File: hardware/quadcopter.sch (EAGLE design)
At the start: 92 parts, among them J1 HEADER-4POS-0.1IN-FEMALE-SMD-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, J2 HEADER-10POSTH-254X10, J3 HEADER-4POS-0.1IN-FEMALE, J4 AVR_SPI_PRG_6-SMD, M1 MOTOR_PADS_GND-MOLEX-SMD, M2 MOTOR_PADS_GND-MOLEX-SMD, M3 MOTOR_PADS_GND-MOLEX-SMD, M4 MOTOR_PADS_GND-MOLEX-SMD, Q1 N-MOSFET-SI2302DS, Q10 N-MOSFET-SI2302DS, Q11 N-MOSFET-SI2302DS, Q12 N-MOSFET-SI2302DS, Q2 N-MOSFET-SI2302DS, Q3 N-MOSFET-SI2302DS, Q4 N-MOSFET-SI2302DS, Q5 N-MOSFET-SI2302DS, Q6 N-MOSFET-SI2302DS, Q7 N-MOSFET-SI2302DS, Q8 N-MOSFET-SI2302DS, Q9 N-MOSFET-SI2302DS, SW1 PUSHBUTTON_-4.5X4.5, U1 ATMEGA128RFA1, U2 IMU_LSM9DS1-LSM9DS1, Y1 CRYSTAL5X3

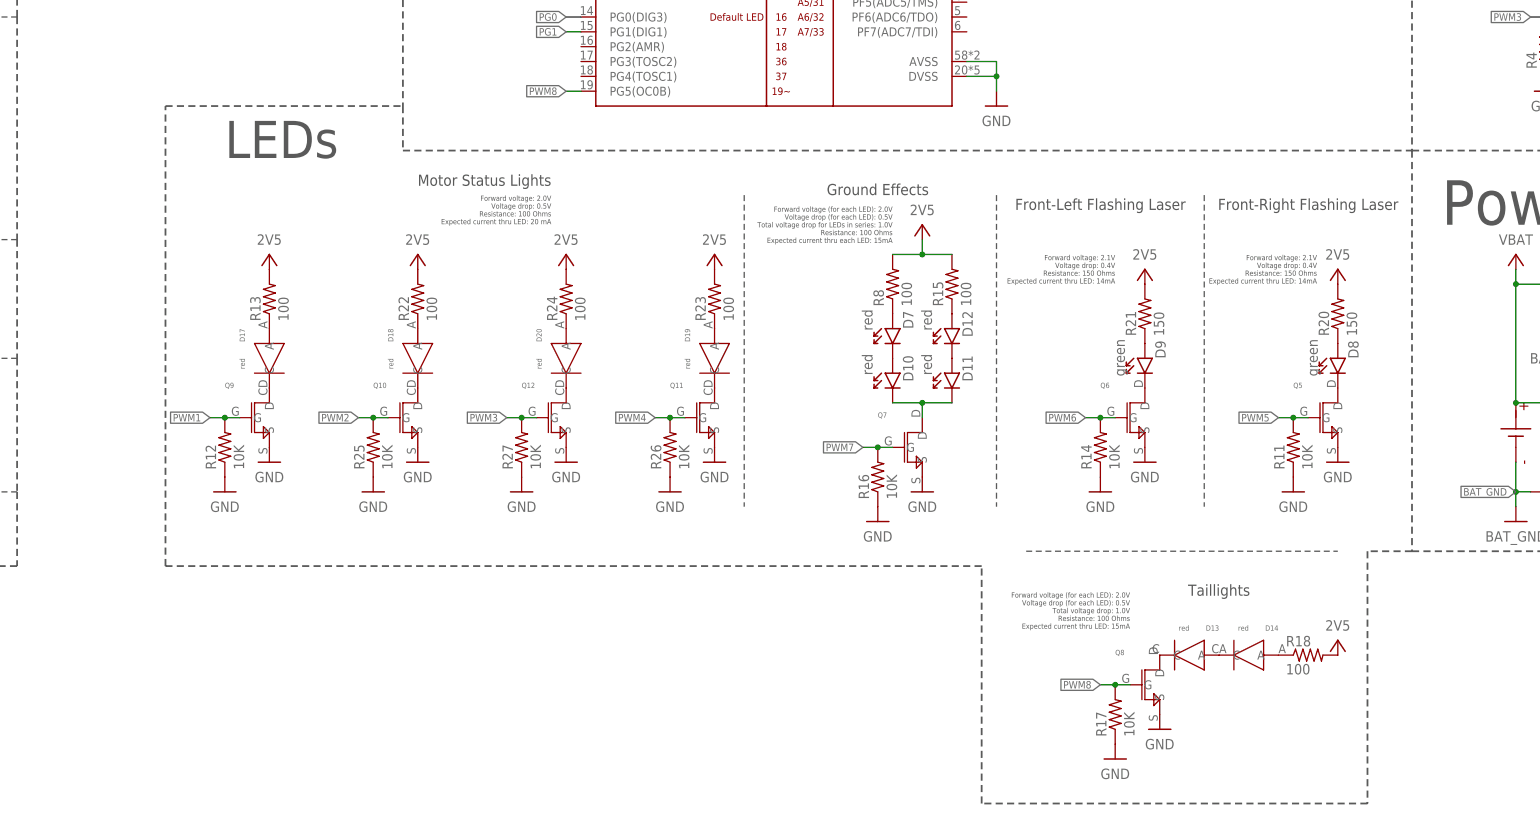
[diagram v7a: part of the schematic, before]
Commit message: Modify LED schematic to meet lab specs
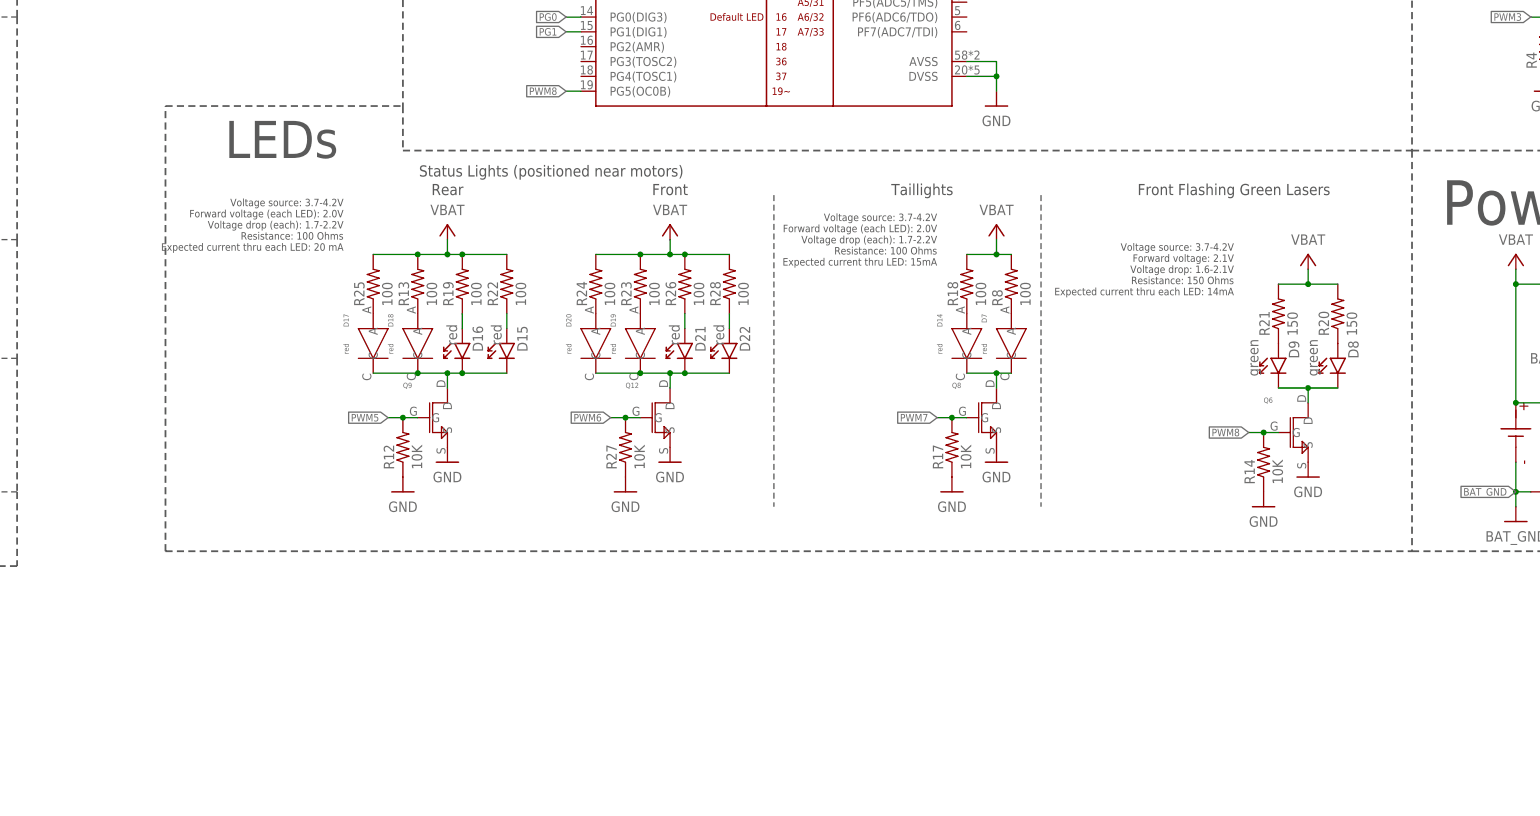
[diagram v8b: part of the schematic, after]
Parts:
- removed D10, D11, D12: red, LED:LED-350-2312-1-ND-REVERSE
- removed D13: red, custom_michael_shao:LED_RED-LTST-C170EKT
- removed Q10, Q11, Q5, Q7: N-MOSFET-SI2302DS, custom_michael_shao:N-MOSFET-SI2302DS
- removed R11, R16: 10K, quadparts_prebuilt_2022:RESISTOR_SMD-2012-0805-10K
- removed R15: 100, quadparts_prebuilt_2022:RESISTOR_SMD-2012-0805-100
- added D15, D16, D21, D22: red, LED:LED-350-2312-1-ND-REVERSE
- added R19, R28: 100, quadparts_prebuilt_2022:RESISTOR_SMD-2012-0805-100
- D7: device LED:LED-350-2312-1-ND-REVERSE -> custom_michael_shao:LED_RED-LTST-C170EKT
- R25, R26: value 10K -> 100; device quadparts_prebuilt_2022:RESISTOR_SMD-2012-0805-10K -> quadparts_prebuilt_2022:RESISTOR_SMD-2012-0805-100
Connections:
- removed net N$18 (its old number): D8.C, Q5.D
- removed net N$21 (its old number): D9.C, Q6.D
- removed net N$28: D11.A, D12.C
- removed net N$29: D13.A, D14.C
- removed net N$30: D10.C, D11.C, Q7.D
- removed net N$32: D13.C, Q8.D
- removed net N$33: D12.A, R15.1
- removed net N$36: D17.A, R13.1
- removed net N$37: D18.A, R22.1
- removed net N$41: D19.C, Q11.D
- new net N$17: D8.C, D9.C, Q6.D
- new net N$24: D17.A, R25.1
- new net N$25: D18.A, R13.1
- new net N$26: D16.A, R19.1
- new net N$34: D15.A, R22.1
- new net N$43: D22.A, R28.1
- net 2V5: no longer R13.2, R15.2, R18.2, R20.2, R21.2, R22.2, R23.2, R24.2, R8.2
- net GND: no longer Q10.S, Q11.S, Q5.S, Q7.S, R11.1, R16.1, R25.1, R26.1
- net N$27: now also D14.C, Q8.D; no longer D10.A
- net N$35: now also D15.C, D16.C, D18.C
- net N$40: now also D19.C, D20.C, D21.C, D22.C, Q12.D; no longer D18.C, Q10.D
- net N$42: now also D21.A, R26.1; no longer D20.C, Q12.D
- net PWM1: no longer Q9.G, R12.2
- net PWM2: no longer Q10.G, R25.2
- net PWM3: no longer Q12.G, R27.2
- net PWM4: no longer Q11.G, R26.2
- net PWM5: now also Q9.G, R12.2; no longer Q5.G, R11.2
- net PWM6: now also Q12.G, R27.2; no longer Q6.G, R14.2
- net PWM7: now also Q8.G, R17.2; no longer Q7.G, R16.2
- net PWM8: now also Q6.G, R14.2; no longer Q8.G, R17.2
- net VBAT: now also R13.2, R18.2, R19.2, R20.2, R21.2, R22.2, R23.2, R24.2, R25.2, R26.2, R28.2, R8.2
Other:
- note added: "Front"
- note added: "Front Flashing Green Lasers"
- note added: "Rear"
- note added: "Status Lights (positioned near motors)"
- note added: "Voltage source: 3.7-4.2V Forward voltage (each LED): 2.0V Voltage drop (each): 1.7-2.2V Resistance: 100 Ohms Expected current thru LED: 15mA"
- note added: "Voltage source: 3.7-4.2V Forward voltage (each LED): 2.0V Voltage drop (each): 1.7-2.2V Resistance: 100 Ohms Expected current thru each LED: 20 mA"
- note added: "Voltage source: 3.7-4.2V Forward voltage: 2.1V Voltage drop: 1.6-2.1V Resistance: 150 Ohms Expected current thru each LED: 14mA"
- note removed: "Forward voltage (for each LED): 2.0V Voltage drop (for each LED): 0.5V Total voltage drop for LEDs in series: 1.0V Resistance: 100 Ohms Expected current thru each LED: 15mA"
- note removed: "Forward voltage (for each LED): 2.0V Voltage drop (for each LED): 0.5V Total voltage drop: 1.0V Resistance: 100 Ohms Expected current thru LED: 15mA"
- note removed: "Forward voltage: 2.0V Voltage drop: 0.5V Resistance: 100 Ohms Expected current thru LED: 20 mA"
- note removed: "Forward voltage: 2.1V Voltage drop: 0.4V Resistance: 150 Ohms Expected current thru LED: 14mA"
- note removed: "Front-Left Flashing Laser"
- note removed: "Front-Right Flashing Laser"
- note removed: "Ground Effects"
- note removed: "Motor Status Lights"
- moved on the sheet: D14, D17, D18, D19, D20, D9, Q12, Q6, Q8, Q9, R12, R13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
